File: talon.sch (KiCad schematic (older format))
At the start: 1 part

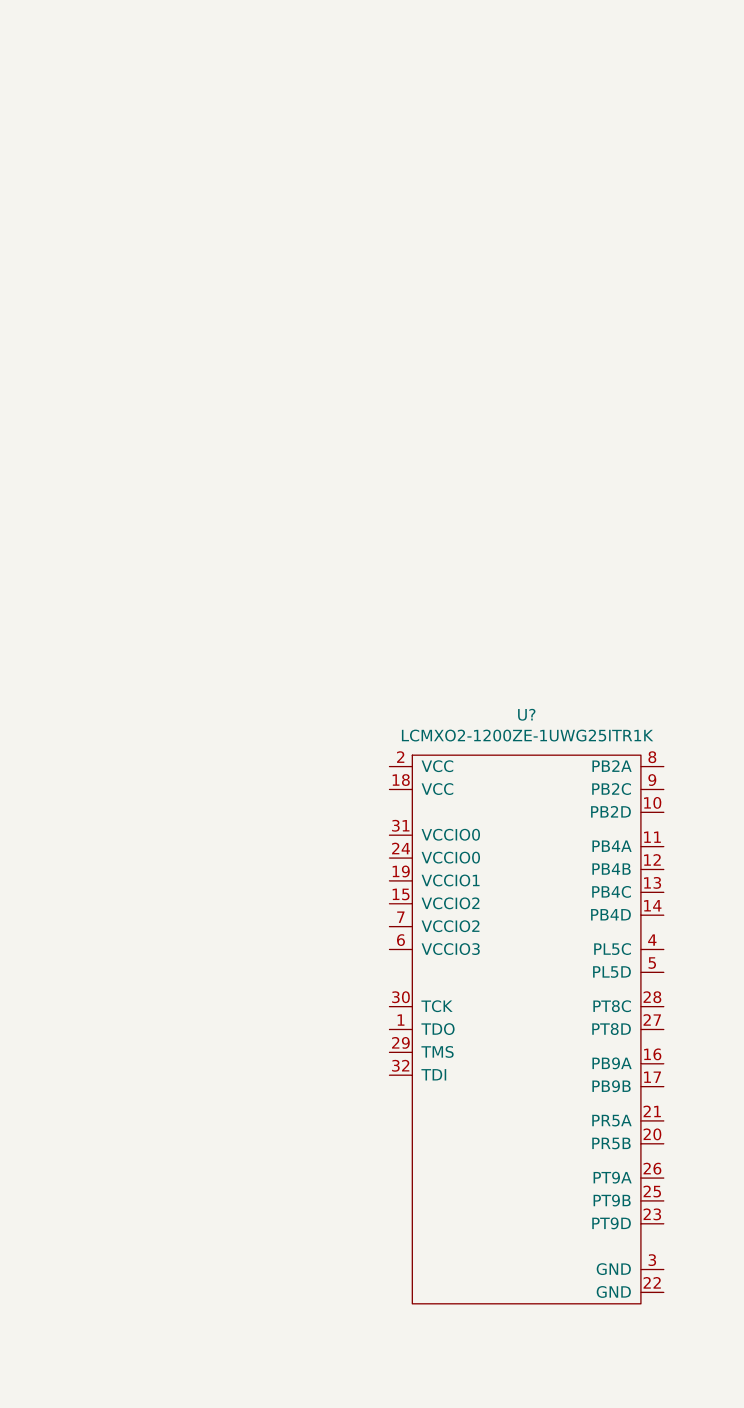
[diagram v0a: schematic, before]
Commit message: Changed MO2 symbol
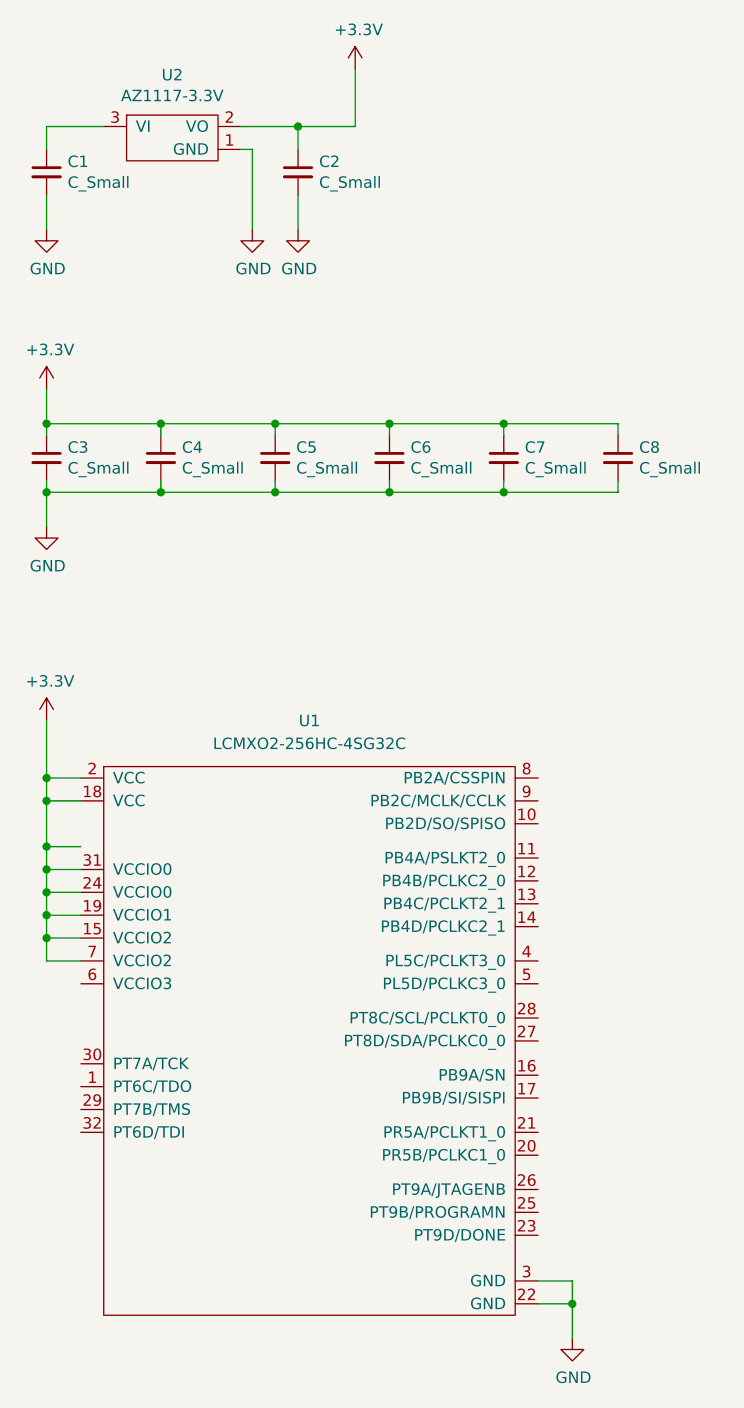
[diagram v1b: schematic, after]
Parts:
- removed U?: LCMXO2-1200ZE-1UWG25ITR1K, symbol talon:LCMXO2-1200ZE-1UWG25ITR1K
- added C1, C2, C3, C4, C5, C6, C7, C8: C_Small, symbol Device:C_Small
- added U1: LCMXO2-256HC-4SG32C, symbol talon:LCMXO2-256HC-4SG32C
- added U2: AZ1117-3.3V, symbol talon:AZ1117-3.3V
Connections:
- new net: C1.1, U2.3 (VI)
- new net +3V3: C2.1, C3.1, C4.1, C5.1, C6.1, C7.1, C8.1, U1.15 (VCCIO2), U1.18 (VCC), U1.19 (VCCIO1), U1.2 (VCC), U1.24 (VCCIO0), U1.31 (VCCIO0), U1.7 (VCCIO2), U2.2 (VO)
- new net GND: C1.2, C2.2, C3.2, C4.2, C5.2, C6.2, C7.2, C8.2, U1.22 (GND), U1.3 (GND), U2.1 (GND)

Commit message: FPGA wired and ready
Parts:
- removed C3, C4: C_Small, symbol Device:C_Small
- added C10, C7, C8, C9: C_Small, symbol Device:C_Small
- added J1: Conn_01x05_Male, symbol Connector:Conn_01x05_Male
- added J2, J3: Conn_01x10_Male, symbol Connector:Conn_01x10_Male
- added J4: USB_B_Micro, symbol Connector:USB_B_Micro
- renumbered C7 to C3, C8 to C4
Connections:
- net +3V3: now also U1.6 (VCCIO3), C10.1, C7.1, C8.1, C9.1, J2.1 (Pin_1), J3.1 (Pin_1)
- net GND: now also C10.2, C7.2, C8.2, C9.2, J1.5 (Pin_5), J2.10 (Pin_10), J3.10 (Pin_10), J4.5 (GND), J4.6 (Shield)
- net at C1.1, U2.3 (VI): now also J4.1 (VBUS)
- net LCMX02_TDO: now reaches U1.1 (PT6C/TDO)
- net LCMX02_TDO: now also J1.2 (Pin_2)
- net LCMX02_PB2D: now reaches U1.10 (PB2D/SO/SPISO)
- net LCMX02_PB2D: now also J2.4 (Pin_4)
- net LCMX02_PB4A: now reaches U1.11 (PB4A/PSLKT2_0)
- net LCMX02_PB4A: now also J2.5 (Pin_5)
- net LCMX02_PB4B: now reaches U1.12 (PB4B/PCLKC2_0)
- net LCMX02_PB4B: now also J2.6 (Pin_6)
- net LCMX02_PB4C: now reaches U1.13 (PB4C/PCLKT2_1)
- net LCMX02_PB4C: now also J2.7 (Pin_7)
- net LCMX02_PB4D: now reaches U1.14 (PB4D/PCLKC2_1)
- net LCMX02_PB4D: now also J2.8 (Pin_8)
- net LCMX02_PB9A: now reaches U1.16 (PB9A/SN)
- net LCMX02_PB9B: now reaches U1.17 (PB9B/SI/SISPI)
- net LCMX02_PR5B: now reaches U1.20 (PR5B/PCLKC1_0)
- net LCMX02_PR5B: now also J3.2 (Pin_2), J3.4 (Pin_4)
- net LCMX02_PR5A: now reaches U1.21 (PR5A/PCLKT1_0)
- net LCMX02_PR5A: now also J2.9 (Pin_9), J3.3 (Pin_3)
- net LCMX02_PT9D: now reaches U1.23 (PT9D/DONE)
- net LCMX02_PT9D: now also J3.7 (Pin_7)
- net LCMX02_PT9B: now reaches U1.25 (PT9B/PROGRAMN)
- net LCMX02_PT9B: now also J3.6 (Pin_6)
- net LCMX02_PT9A: now reaches U1.26 (PT9A/JTAGENB)
- net LCMX02_PT9A: now also J3.5 (Pin_5)
- net LCMX02_PT8D: now reaches U1.27 (PT8D/SDA/PCLKC0_0)
- net LCMX02_PT8D: now also J3.9 (Pin_9)
- net LCMX02_PT8C: now reaches U1.28 (PT8C/SCL/PCLKT0_0)
- net LCMX02_PT8C: now also J3.8 (Pin_8)
- net LCMX02_TMS: now reaches U1.29 (PT7B/TMS)
- net LCMX02_TMS: now also J1.3 (Pin_3)
- net LCMX02_TCK: now reaches U1.30 (PT7A/TCK)
- net LCMX02_TCK: now also J1.1 (Pin_1)
- net LCMX02_TDI: now reaches U1.32 (PT6D/TDI)
- net LCMX02_TDI: now also J1.4 (Pin_4)
- net LCMX02_PB5C: now reaches U1.4 (PL5C/PCLKT3_0)
- net LCMX02_PB5D: now reaches U1.5 (PL5D/PCLKC3_0)
- net LCMX02_PB2A: now reaches U1.8 (PB2A/CSSPIN)
- net LCMX02_PB2A: now also J2.2 (Pin_2)
- net LCMX02_PB2C: now reaches U1.9 (PB2C/MCLK/CCLK)
- net LCMX02_PB2C: now also J2.3 (Pin_3)
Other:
- moved on the sheet: C1, C2, C3, C4, U2
